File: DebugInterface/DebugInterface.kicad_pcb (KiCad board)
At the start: 2 copper layers, 157 x 175.6 mm, 54 parts, among them J1 IDC-16M, J10 IDC-16M, J11 IDC-16M, J12 IDC-16M, J13 IDC-16M, J14 IDC-16M, J15 IDC-16M, J16 IDC-16M, J17 IDC-16M, J18 IDC-16M, J19 IDC-16M, J2 IDC-16M, J20 IDC-16M, J21 IDC-16M, J22 IDC-16M, J23 IDC-16M, J24 IDC-16M, J25 USB_B, J26 ISP, J27 Barrel_Jack_MountingPin, J3 IDC-16M, J4 IDC-16M, J5 IDC-16M, J6 IDC-16M, J7 IDC-16M, J8 IDC-16M, J9 IDC-16M, U1 8255, U10 PIC18F2550-ISO, U2 8255, U3 8255, U4 8255, U5 8255, U6 8255, U7 8255, U8 8255, U9 74LS138, Y1 20MHz

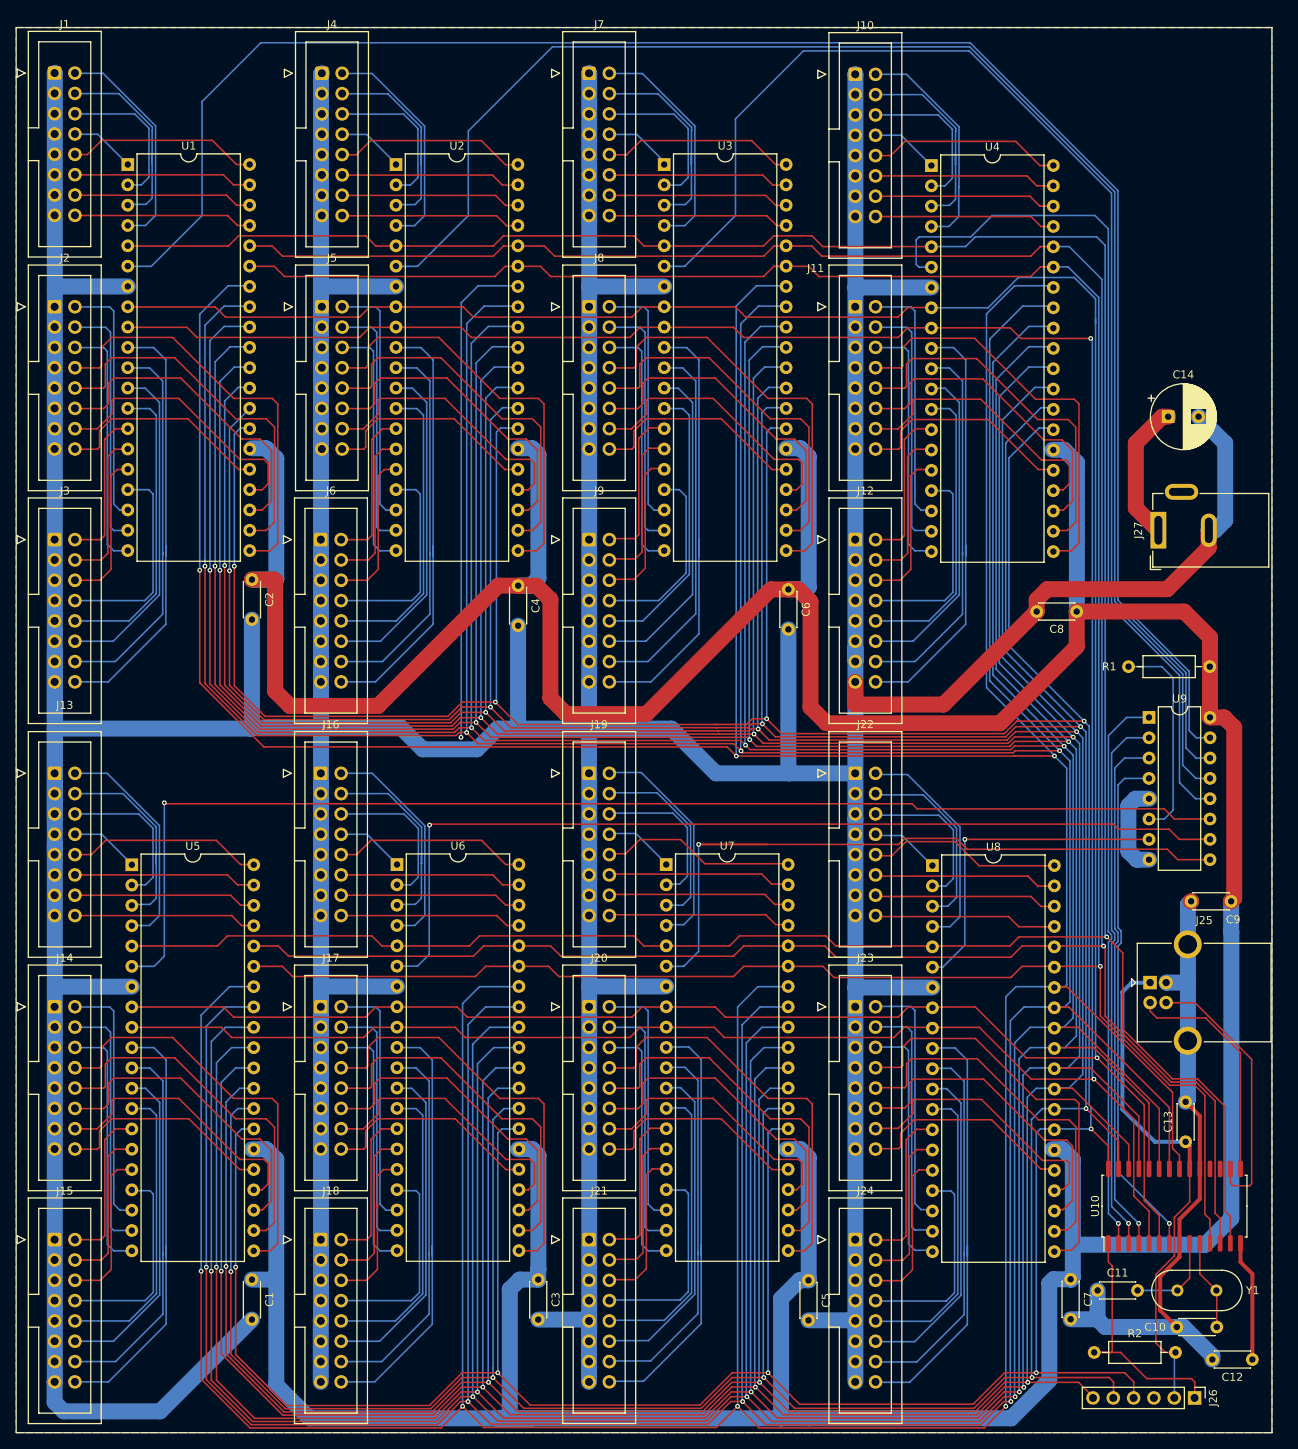
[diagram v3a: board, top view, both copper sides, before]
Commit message: DebugInterface: better PCB routing
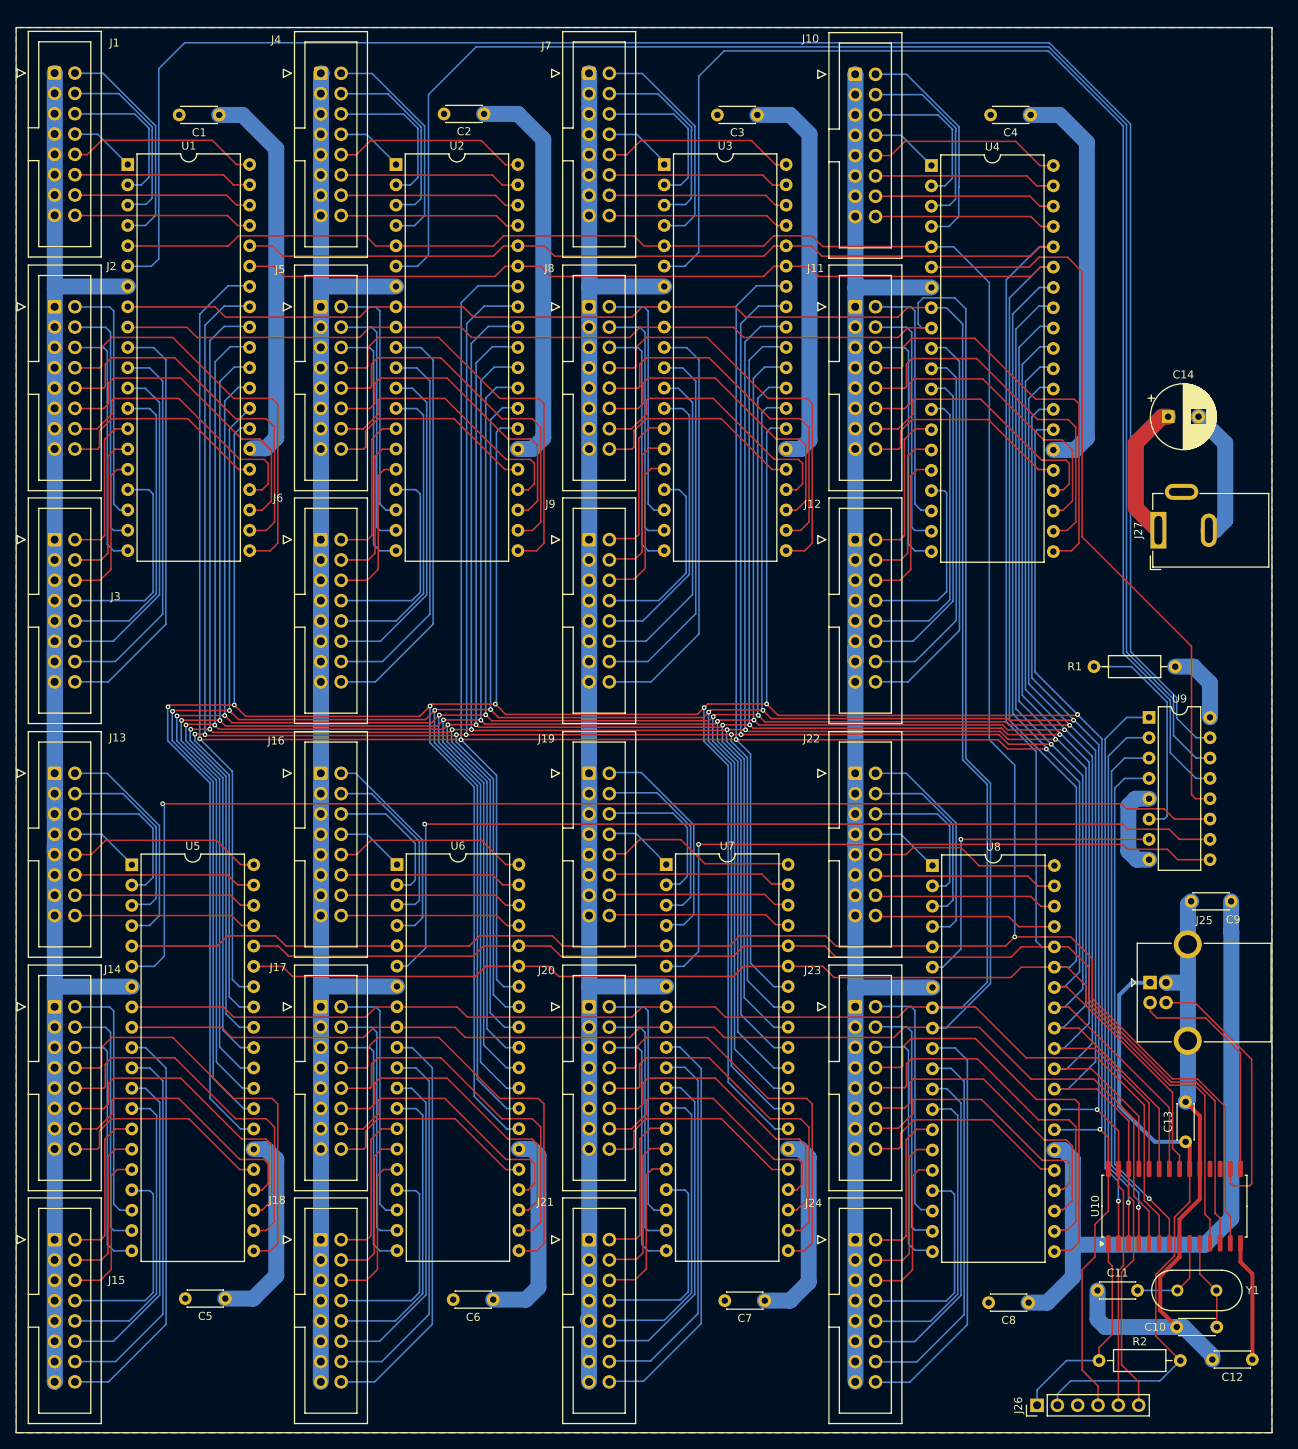
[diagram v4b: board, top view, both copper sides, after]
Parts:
- moved C3 148.1 mm to (107.7, 28.6), turned to 180 degrees
- moved C1 145.6 mm to (40.4, 28.6), turned to 180 degrees
- moved C6 96.1 mm to (74.6, 176.7), turned to 180 degrees
- moved C4 87.0 mm to (141.8, 28.6), turned to 180 degrees
- moved C8 86.6 mm to (141.6, 177.0)
- moved C5 72.9 mm to (41.1, 176.5), turned to 180 degrees
- moved C2 65.0 mm to (73.5, 28.4), turned to 180 degrees
- moved C7 38.3 mm to (108.6, 176.8), turned to 180 degrees
- moved J26 19.7 mm to (142.6, 189.9), turned to 90 degrees
- moved R1 4.32 mm to (159.9, 97.5)
- moved R2 1.18 mm to (150.4, 184.3)
- moved J4 0.13 mm to (53.1, 23.4)
- moved J5 0.13 mm to (53.1, 52.6)
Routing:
- net GND: track 1124.7 -> 869.7 mm
- net VCC: track 635.7 -> 385.9 mm
- net /D0: track 754.6 -> 521.6 mm, vias 8 -> 4
- net /D1: track 728.0 -> 519.5 mm, vias 8 -> 7
- net /D2: track 701.5 -> 517.8 mm, vias 8 -> 7
- net /D3: track 675.5 -> 516.3 mm, vias 8 -> 7
- net /D4: track 647.0 -> 513.8 mm, vias 8 -> 7
- net /D5: track 626.9 -> 543.1 mm, vias 8 -> 7
- net /D6: track 601.1 -> 535.6 mm, vias 9 -> 8
- net /D7: track 578.9 -> 536.2 mm, vias 9 -> 8
- net /A4: track 375.0 -> 352.8 mm, vias 1 -> 0
- net /~{RD}: track 384.8 -> 365.1 mm
- net /~{CS3}: track 108.6 -> 93.7 mm
- net Net-(J25-VBUS): track 63.7 -> 77.6 mm
- net /~{CS2}: track 160.8 -> 172.4 mm
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
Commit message: DebugInterface: Add some LEDs
Some indicator LEDs: power, reset, activity.
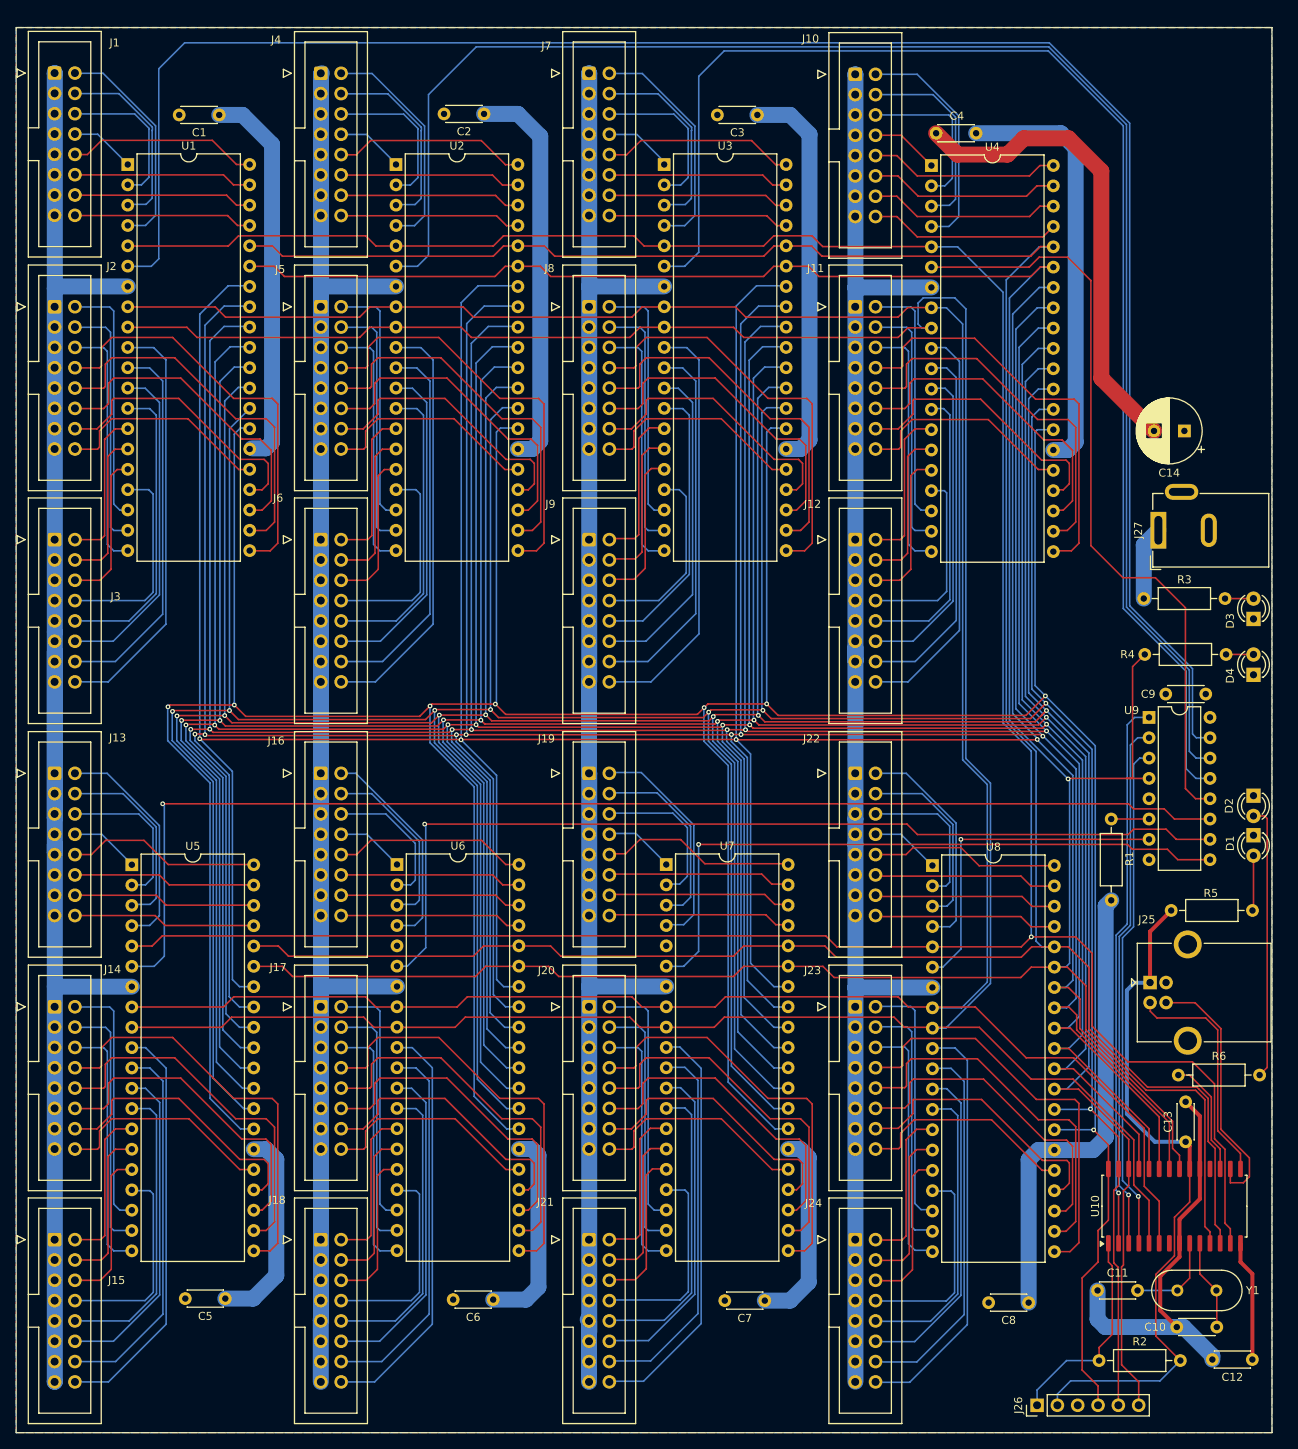
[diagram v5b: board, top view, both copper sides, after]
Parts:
- added D1: LED, LED_THT:LED_D3.0mm, F.Cu at (169.7, 118.6)
- added D2: LED, LED_THT:LED_D3.0mm, F.Cu at (169.7, 113.7)
- added D3: LED, LED_THT:LED_D3.0mm, F.Cu at (169.7, 91.6)
- added D4: LED, LED_THT:LED_D3.0mm, F.Cu at (169.7, 98.6)
- added R3: 1K, Resistor_THT:R_Axial_DIN0207_L6.3mm_D2.5mm_P10.16mm_Horizontal, F.Cu at (156.0, 89.0)
- added R4: 1K, Resistor_THT:R_Axial_DIN0207_L6.3mm_D2.5mm_P10.16mm_Horizontal, F.Cu at (156.1, 96.0)
- added R5: 1K, Resistor_THT:R_Axial_DIN0207_L6.3mm_D2.5mm_P10.16mm_Horizontal, F.Cu at (159.4, 128.0)
- added R6: 1K, Resistor_THT:R_Axial_DIN0207_L6.3mm_D2.5mm_P10.16mm_Horizontal, F.Cu at (160.3, 148.6)
- moved R1 30.3 mm to (151.9, 126.7), turned to 90 degrees
- moved C9 26.1 mm to (163.7, 101.0)
- moved C4 7.19 mm to (135.0, 30.9)
- moved C14 2.70 mm to (161.0, 68.1), turned to 180 degrees
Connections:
- U10 pad 17: unconnected-(U10-TX/CK/RC6-Pad17) -> Net-(U10-TX/CK/RC6)
- U10 pad 7: /~{AEN} -> unconnected-(U10-RA5/AN4/~{SS}/HLVDIN/C2OUT-Pad7)
- U9 pad 4: /~{AEN} -> /RST
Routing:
- net /~{AEN}: track 64.5 -> 0.00 mm, vias 1 -> 0
- net VCC: track 385.9 -> 343.9 mm
- net Net-(D2-A): track 0.00 -> 34.3 mm
- net /RST: track 348.5 -> 376.4 mm, vias 0 -> 1
- net Net-(U9-E3): track 27.6 -> 4.72 mm
- net Net-(U10-TX/CK/RC6): track 0.00 -> 14.7 mm
- net Net-(J25-VBUS): track 77.6 -> 86.7 mm
- net Net-(D1-A): track 0.00 -> 6.91 mm
- net /D5: track 543.1 -> 538.2 mm
- net /D4: track 513.8 -> 509.6 mm
- net /D3: track 516.3 -> 512.4 mm
- net /D7: track 536.2 -> 532.3 mm
- net /D6: track 535.6 -> 532.0 mm
- net Net-(D3-A): track 0.00 -> 3.56 mm
- net Net-(D4-A): track 0.00 -> 3.43 mm
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
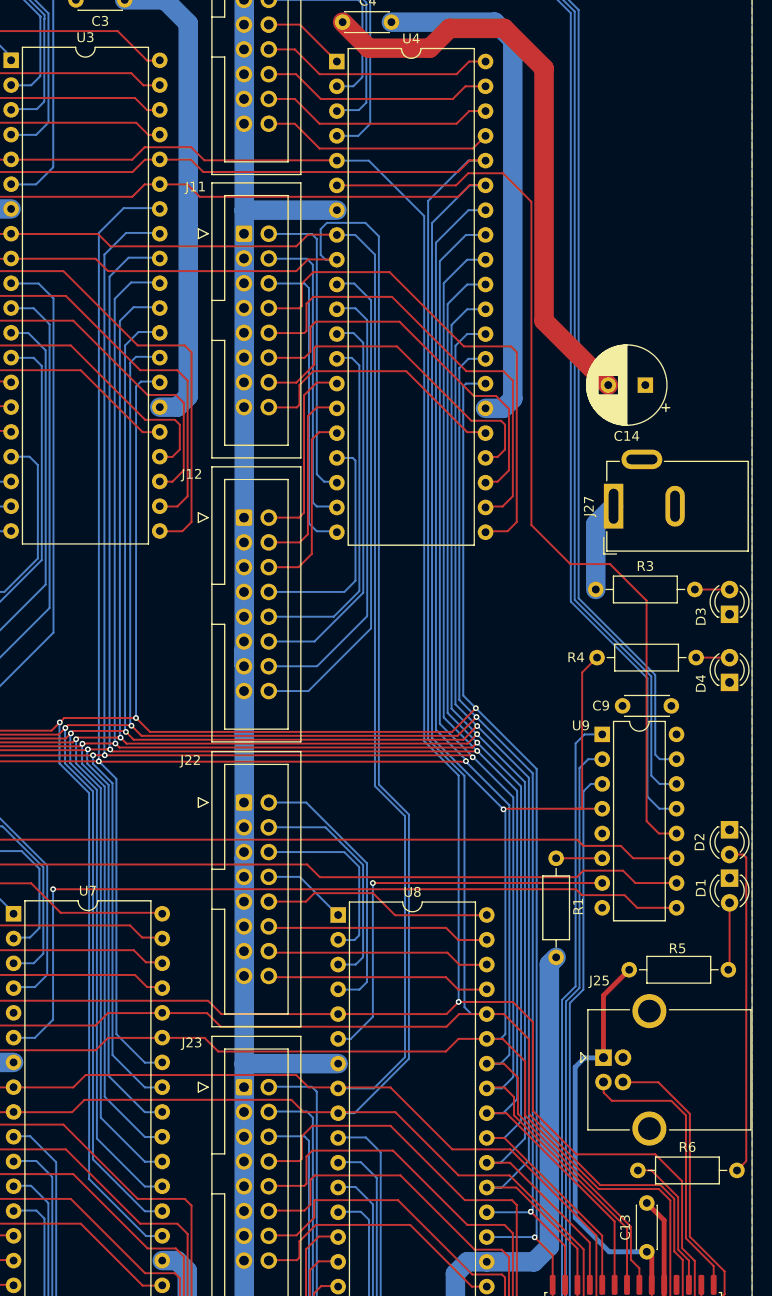
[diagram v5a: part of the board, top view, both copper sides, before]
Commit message: DebugInterface: Final preps
A bit of layout optimization, LED designations on silkscreen
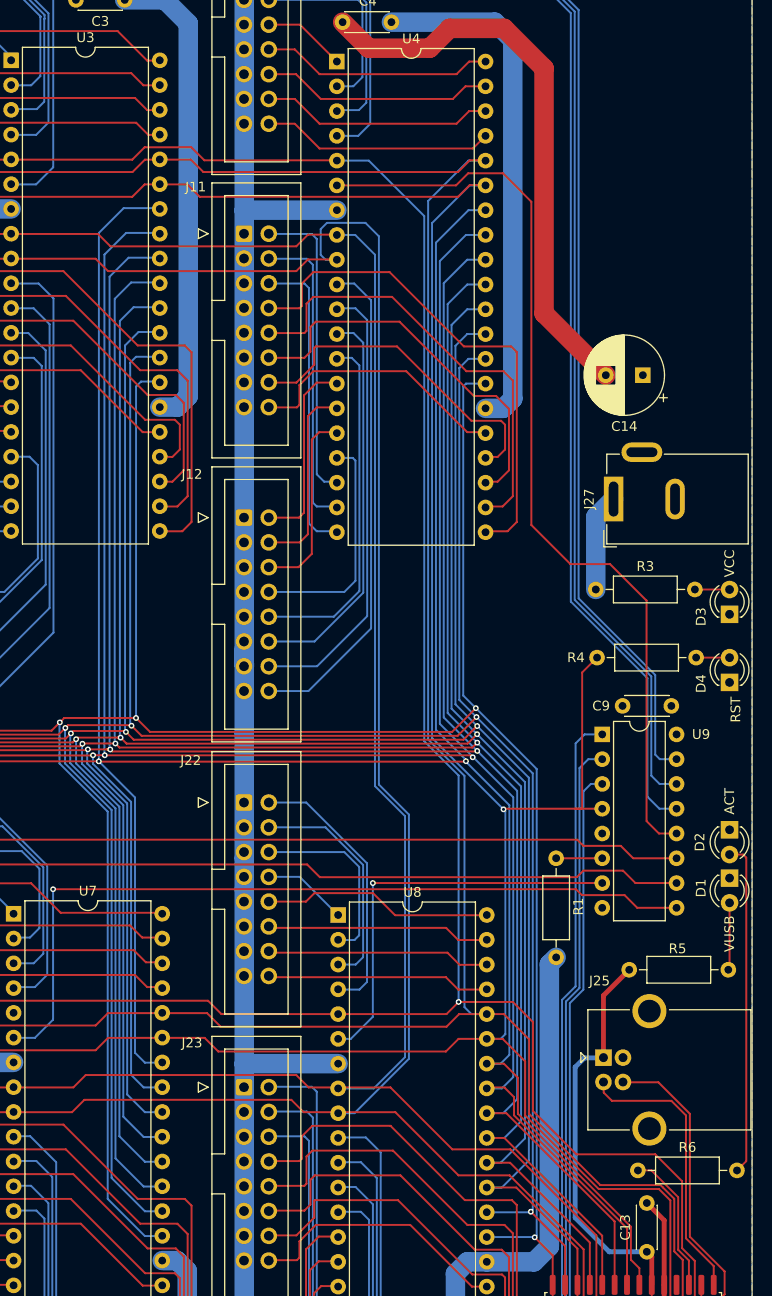
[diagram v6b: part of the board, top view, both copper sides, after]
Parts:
- D1: value LED -> VUSB
- D2: value LED -> ACT
- D3: value LED -> VCC
- D4: value LED -> RST
- moved C14 1.05 mm to (160.8, 67.1)
- moved J27 0.74 mm to (157.8, 79.8)
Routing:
- net GND: track 872.5 -> 871.4 mm
- net VCC: track 343.9 -> 344.6 mm
